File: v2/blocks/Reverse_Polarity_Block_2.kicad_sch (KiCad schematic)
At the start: 5 parts, among them Q6 AP25P06K

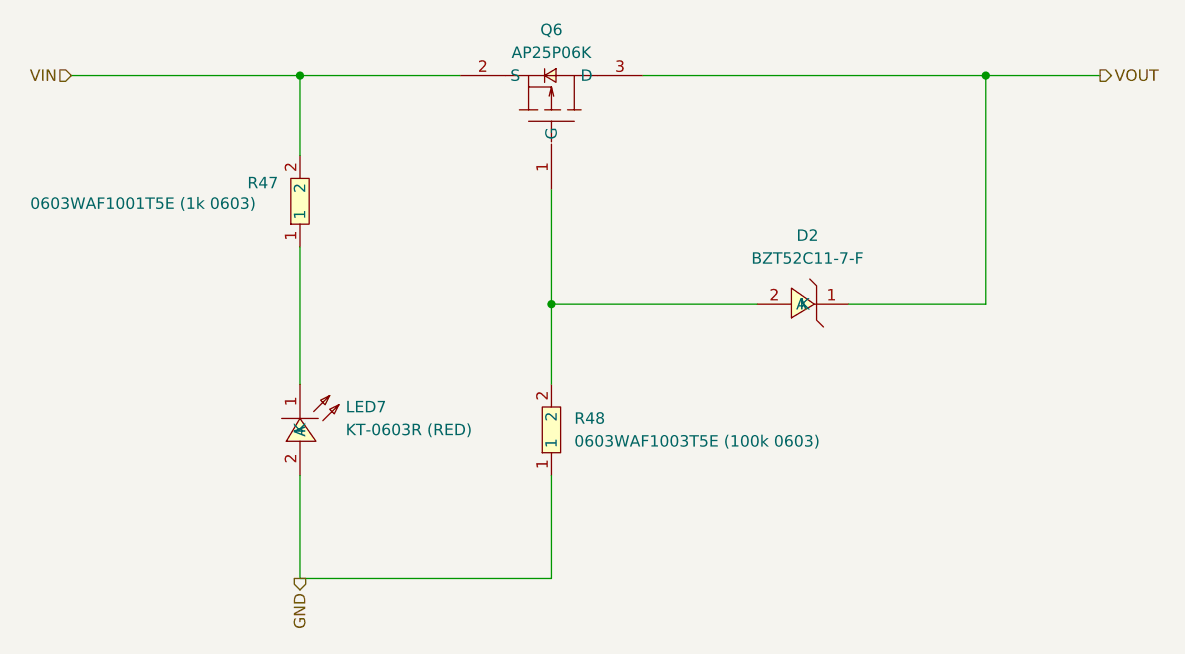
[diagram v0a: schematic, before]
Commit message: preliminary layout
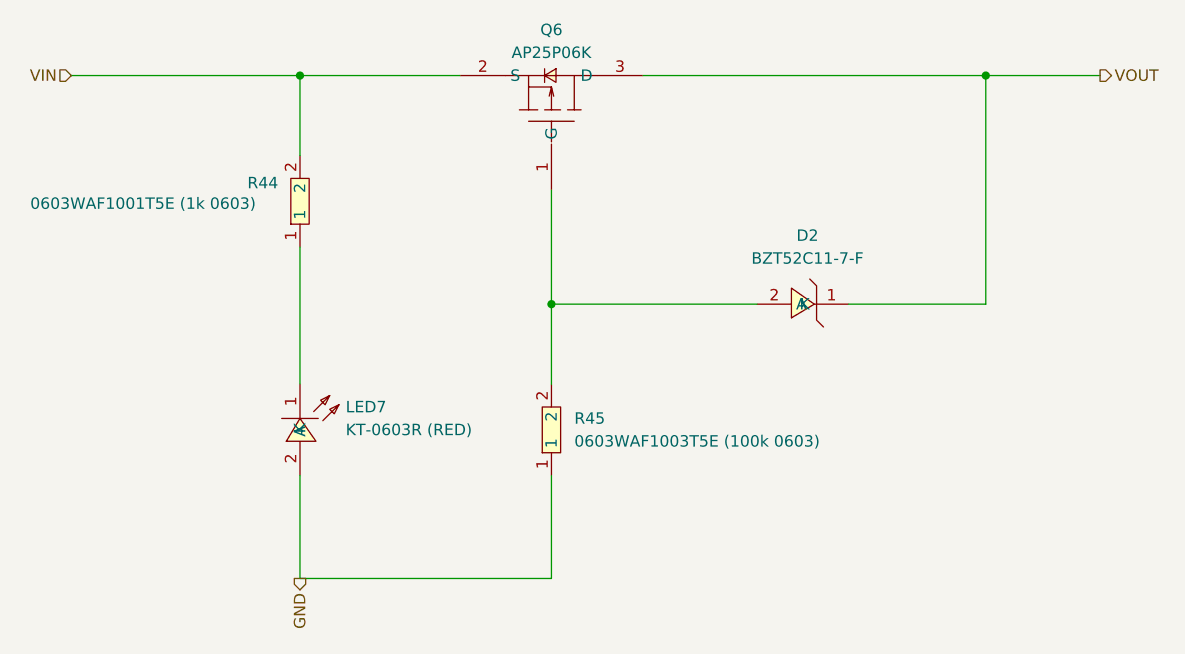
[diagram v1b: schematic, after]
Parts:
- renumbered R47 to R44, R48 to R45
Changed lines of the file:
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@@
 		(dnp no)
 		(fields_autoplaced yes)
-		(property "Reference" "R48"
+		(property "Reference" "R45"
 			(at 132.08 101.5999 90)
 			(effects
@@
 			(project "EPSv2"
 				(path "/61d36b12-c329-4dd2-b08b-b63678fc7b25/fd2bb6ae-6364-490e-a1d3-a228be8205a2"
-					(reference "R48")
+					(reference "R45")
 					(unit 1)
 				)
@@
 		(on_board yes)
 		(dnp no)
-		(property "Reference" "R47"
+		(property "Reference" "R44"
 			(at 95.758 75.438 90)
 			(effects
@@
 			(project "EPSv2"
 				(path "/61d36b12-c329-4dd2-b08b-b63678fc7b25/fd2bb6ae-6364-490e-a1d3-a228be8205a2"
-					(reference "R47")
-					(unit 1)
-				)
+					(reference "R44")
+					(unit 1)
+				)

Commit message: routing done
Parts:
- renumbered D2 to D6, R44 to R52, R45 to R53
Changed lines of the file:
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@@
 		(dnp no)
 		(fields_autoplaced yes)
-		(property "Reference" "R45"
+		(property "Reference" "R53"
 			(at 132.08 101.5999 90)
 			(effects
@@
 			(project "EPSv2"
 				(path "/61d36b12-c329-4dd2-b08b-b63678fc7b25/fd2bb6ae-6364-490e-a1d3-a228be8205a2"
-					(reference "R45")
+					(reference "R53")
 					(unit 1)
 				)
@@
 		(on_board yes)
 		(dnp no)
-		(property "Reference" "R44"
+		(property "Reference" "R52"
 			(at 95.758 75.438 90)
 			(effects
@@
 			(project "EPSv2"
 				(path "/61d36b12-c329-4dd2-b08b-b63678fc7b25/fd2bb6ae-6364-490e-a1d3-a228be8205a2"
-					(reference "R44")
+					(reference "R52")
 					(unit 1)
 				)
@@
 		(dnp no)
 		(fields_autoplaced yes)
-		(property "Reference" "D2"
+		(property "Reference" "D6"
 			(at 157.99 81.28 0)
 			(effects
@@
 			(project "EPSv2"
 				(path "/61d36b12-c329-4dd2-b08b-b63678fc7b25/fd2bb6ae-6364-490e-a1d3-a228be8205a2"
-					(reference "D2")
-					(unit 1)
-				)
+					(reference "D6")
+					(unit 1)
+				)

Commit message: CAN txrx
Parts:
- renumbered D6 to D8, R52 to R59, R53 to R60
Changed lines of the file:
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@@
 		(shape output)
 		(at 190.5 63.5 0)
-		(fields_autoplaced yes)
 		(effects
 			(font
@@
 		(shape input)
 		(at 76.2 63.5 180)
-		(fields_autoplaced yes)
 		(effects
 			(font
@@
 		(shape output)
 		(at 101.6 119.38 270)
-		(fields_autoplaced yes)
 		(effects
 			(font
@@
 		(dnp no)
 		(fields_autoplaced yes)
-		(property "Reference" "R53"
+		(property "Reference" "R60"
 			(at 132.08 101.5999 90)
 			(effects
@@
 			(project "EPSv2"
 				(path "/61d36b12-c329-4dd2-b08b-b63678fc7b25/fd2bb6ae-6364-490e-a1d3-a228be8205a2"
-					(reference "R53")
+					(reference "R60")
 					(unit 1)
 				)
@@
 		(on_board yes)
 		(dnp no)
-		(property "Reference" "R52"
+		(property "Reference" "R59"
 			(at 95.758 75.438 90)
 			(effects
@@
 			(project "EPSv2"
 				(path "/61d36b12-c329-4dd2-b08b-b63678fc7b25/fd2bb6ae-6364-490e-a1d3-a228be8205a2"
-					(reference "R52")
+					(reference "R59")
 					(unit 1)
 				)
@@
 		(dnp no)
 		(fields_autoplaced yes)
-		(property "Reference" "D6"
+		(property "Reference" "D8"
 			(at 157.99 81.28 0)
 			(effects
@@
 			(project "EPSv2"
 				(path "/61d36b12-c329-4dd2-b08b-b63678fc7b25/fd2bb6ae-6364-490e-a1d3-a228be8205a2"
-					(reference "D6")
+					(reference "D8")
 					(unit 1)
 				)

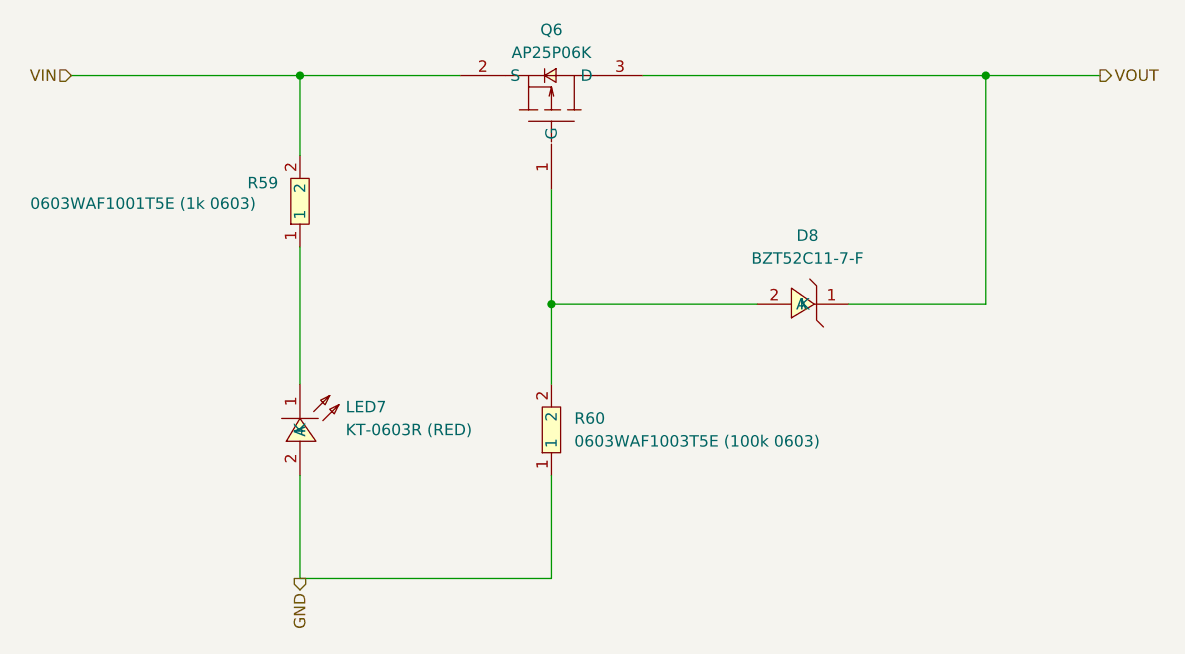
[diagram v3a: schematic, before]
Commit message: can transceiver and battery reverse polarity bypass
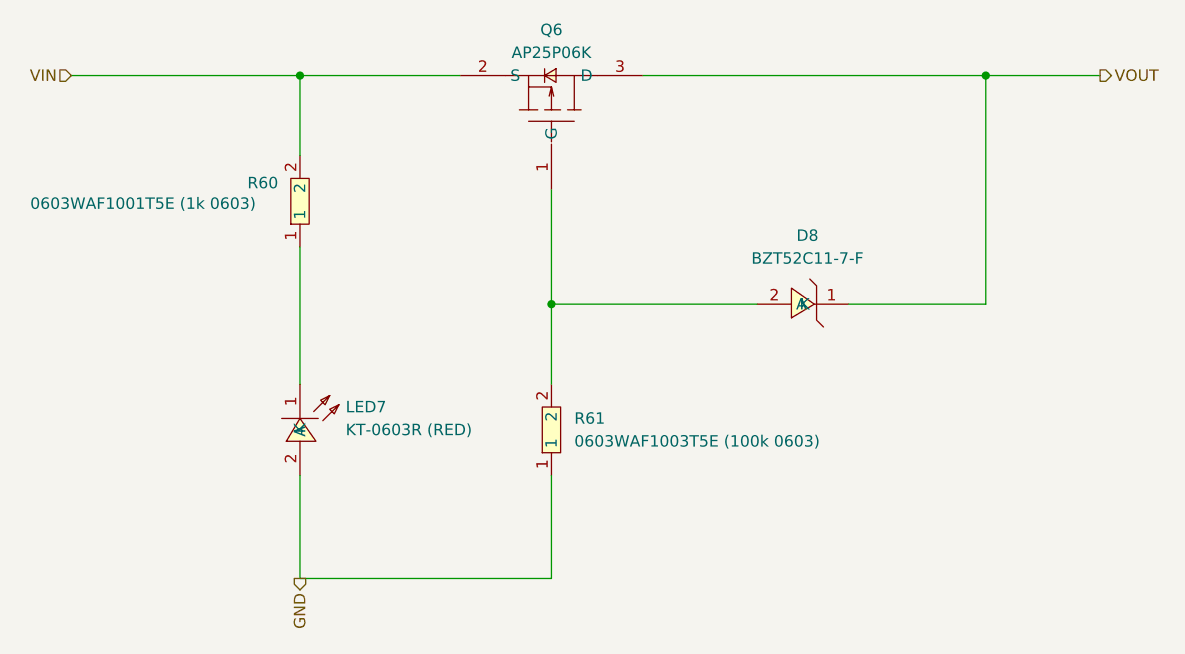
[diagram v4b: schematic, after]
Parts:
- renumbered R59 to R60, R60 to R61
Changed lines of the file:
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@@
 		(shape output)
 		(at 190.5 63.5 0)
+		(fields_autoplaced yes)
 		(effects
 			(font
@@
 		(shape input)
 		(at 76.2 63.5 180)
+		(fields_autoplaced yes)
 		(effects
 			(font
@@
 		(shape output)
 		(at 101.6 119.38 270)
+		(fields_autoplaced yes)
 		(effects
 			(font
@@
 		(dnp no)
 		(fields_autoplaced yes)
-		(property "Reference" "R60"
+		(property "Reference" "R61"
 			(at 132.08 101.5999 90)
 			(effects
@@
 			(project "EPSv2"
 				(path "/61d36b12-c329-4dd2-b08b-b63678fc7b25/fd2bb6ae-6364-490e-a1d3-a228be8205a2"
-					(reference "R60")
+					(reference "R61")
 					(unit 1)
 				)
@@
 		(on_board yes)
 		(dnp no)
-		(property "Reference" "R59"
+		(property "Reference" "R60"
 			(at 95.758 75.438 90)
 			(effects
@@
 			(project "EPSv2"
 				(path "/61d36b12-c329-4dd2-b08b-b63678fc7b25/fd2bb6ae-6364-490e-a1d3-a228be8205a2"
-					(reference "R59")
+					(reference "R60")
 					(unit 1)
 				)

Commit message: bigger current ratings for 5V and 9V
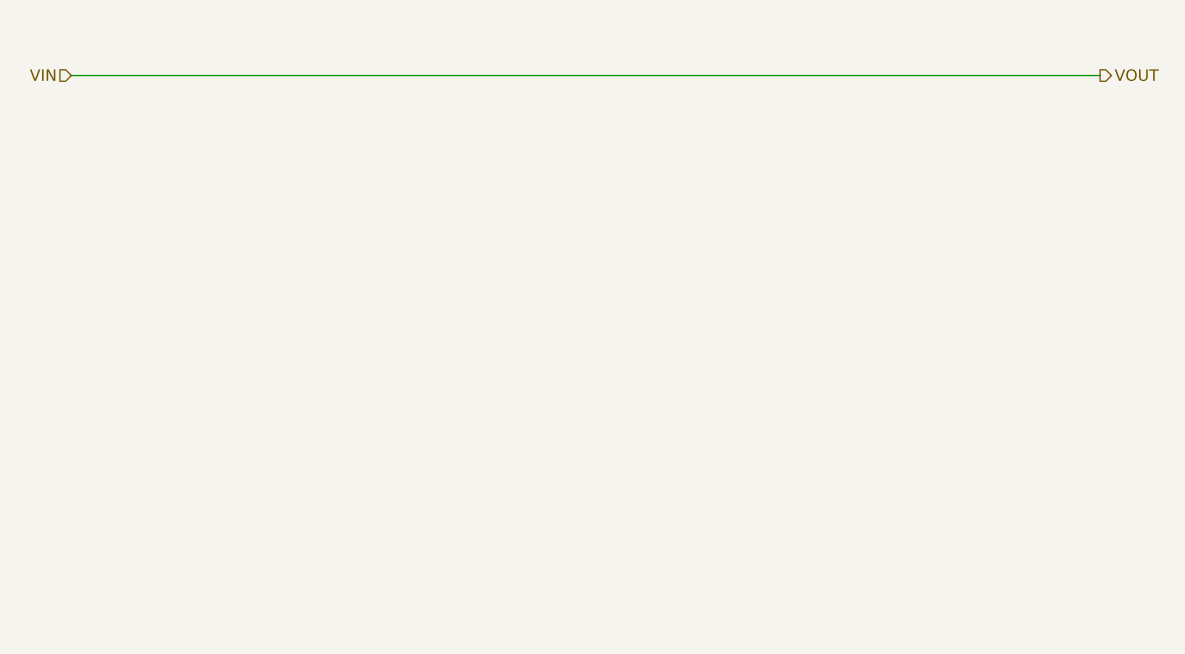
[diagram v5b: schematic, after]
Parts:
- removed D8: BZT52C11-7-F, Rocketry_Easyeda:SOD-123_L2.8-W1.8-LS3.7-RD, symbol Rocketry_Easyeda:BZT52C11-7-F
- removed LED7: KT-0603R (RED), Rocketry_Easyeda:LED0603-RD, symbol Rocketry_Easyeda:KT-0603R
- removed Q6: AP25P06K, Rocketry_Easyeda:TO-252-2_L6.6-W6.1-P4.57-LS10.1-BL, symbol Rocketry_Easyeda:AP25P06K
- removed R60: 0603WAF1001T5E (1k 0603), Rocketry_Easyeda:R0603, symbol Rocketry_Easyeda:0603WAF1001T5E (1k 0603)
- removed R61: 0603WAF1003T5E (100k 0603), Rocketry_Easyeda:R0603, symbol Rocketry_Easyeda:0603WAF1003T5E (100k 0603)
